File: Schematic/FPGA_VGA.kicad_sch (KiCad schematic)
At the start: 16 parts, among them J1 Conn_01x06, U1 Upduino_3.0, Y1 25.175 MHz 7050 3.3V

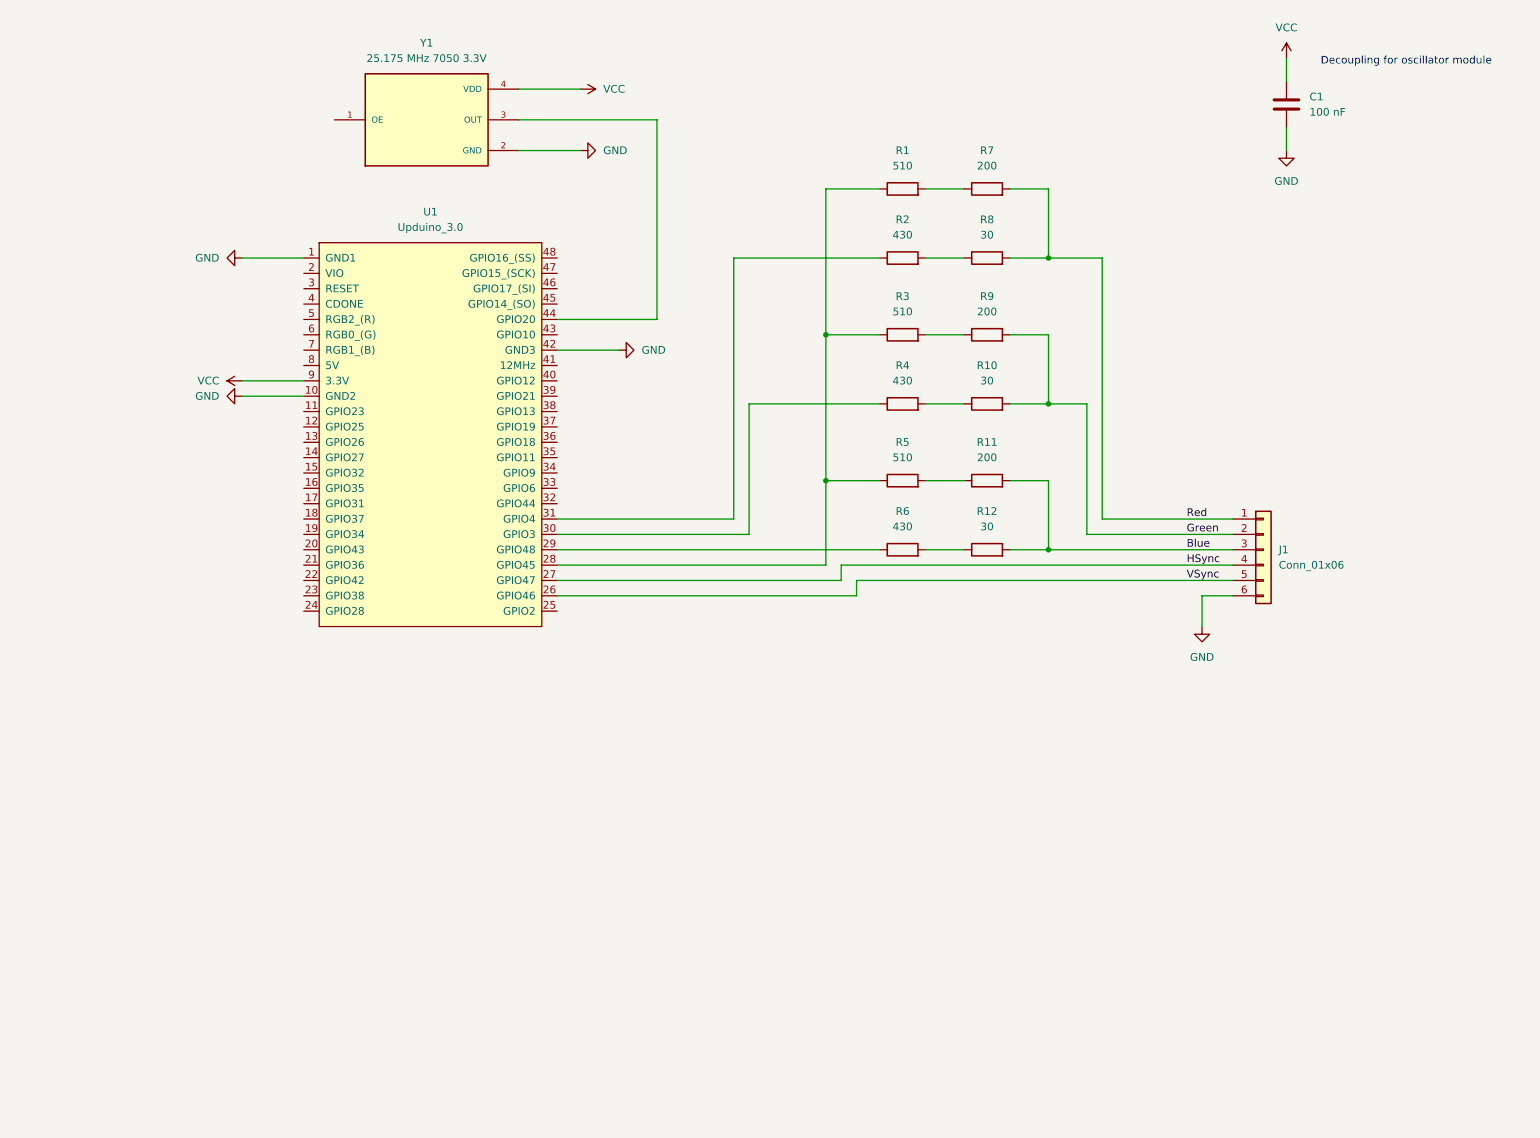
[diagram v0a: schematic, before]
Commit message: start to add level translators for host interface
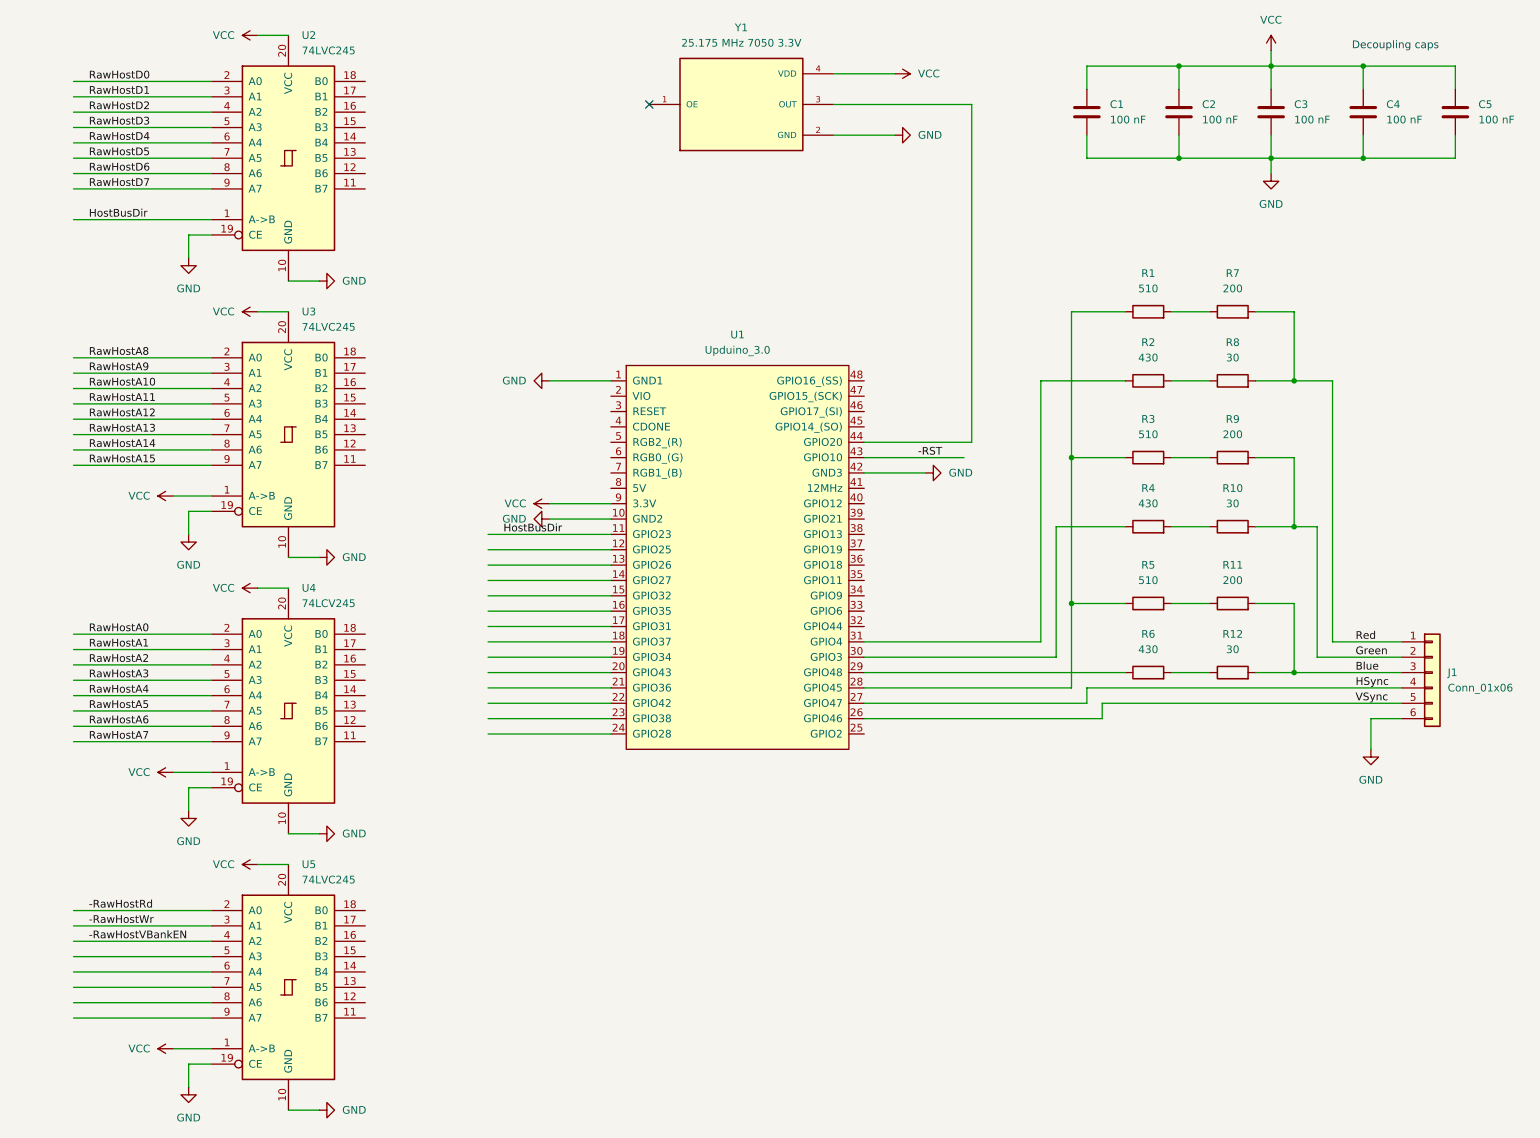
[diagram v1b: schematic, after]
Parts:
- added C2, C3, C4, C5: 100 nF, symbol Device:C
- added U2, U3, U5: 74LVC245, symbol 74xx:74LS245
- added U4: 74LCV245, symbol 74xx:74LS245
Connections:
- net GND: now also C2.2, C3.2, C4.2, C5.2, U2.10 (GND), U2.19 (CE), U3.10 (GND), U3.19 (CE), U4.10 (GND), U4.19 (CE), U5.10 (GND), U5.19 (CE)
- net VCC: now also C2.1, C3.1, C4.1, C5.1, U2.20 (VCC), U3.1 (A->B), U3.20 (VCC), U4.1 (A->B), U4.20 (VCC), U5.1 (A->B), U5.20 (VCC)
- net HostBusDir: now reaches U1.11 (GPIO23)
- net HostBusDir: now also U2.1 (A->B)
- net -RST: now reaches U1.43 (GPIO10)
- new net -RawHostRd: U5.2 (A0)
- new net -RawHostVBankEN: U5.4 (A2)
- new net -RawHostWr: U5.3 (A1)
- new net RawHostA0: U4.2 (A0)
- new net RawHostA1: U4.3 (A1)
- new net RawHostA10: U3.4 (A2)
- new net RawHostA11: U3.5 (A3)
- new net RawHostA12: U3.6 (A4)
- new net RawHostA13: U3.7 (A5)
- new net RawHostA14: U3.8 (A6)
- new net RawHostA15: U3.9 (A7)
- new net RawHostA2: U4.4 (A2)
- new net RawHostA3: U4.5 (A3)
- new net RawHostA4: U4.6 (A4)
- new net RawHostA5: U4.7 (A5)
- new net RawHostA6: U4.8 (A6)
- new net RawHostA7: U4.9 (A7)
- new net RawHostA8: U3.2 (A0)
- new net RawHostA9: U3.3 (A1)
- new net RawHostD0: U2.2 (A0)
- new net RawHostD1: U2.3 (A1)
- new net RawHostD2: U2.4 (A2)
- new net RawHostD3: U2.5 (A3)
- new net RawHostD4: U2.6 (A4)
- new net RawHostD5: U2.7 (A5)
- new net RawHostD6: U2.8 (A6)
- new net RawHostD7: U2.9 (A7)
- no-connect marks 0 -> 1
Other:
- note added: "Decoupling caps"
- note removed: "Decoupling for oscillator module"
- moved on the sheet: C1, J1, R1, R10, R11, R12, R2, R3, R4, R5, R6, R7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

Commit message: added a host interface
Also, modularized the schematic.
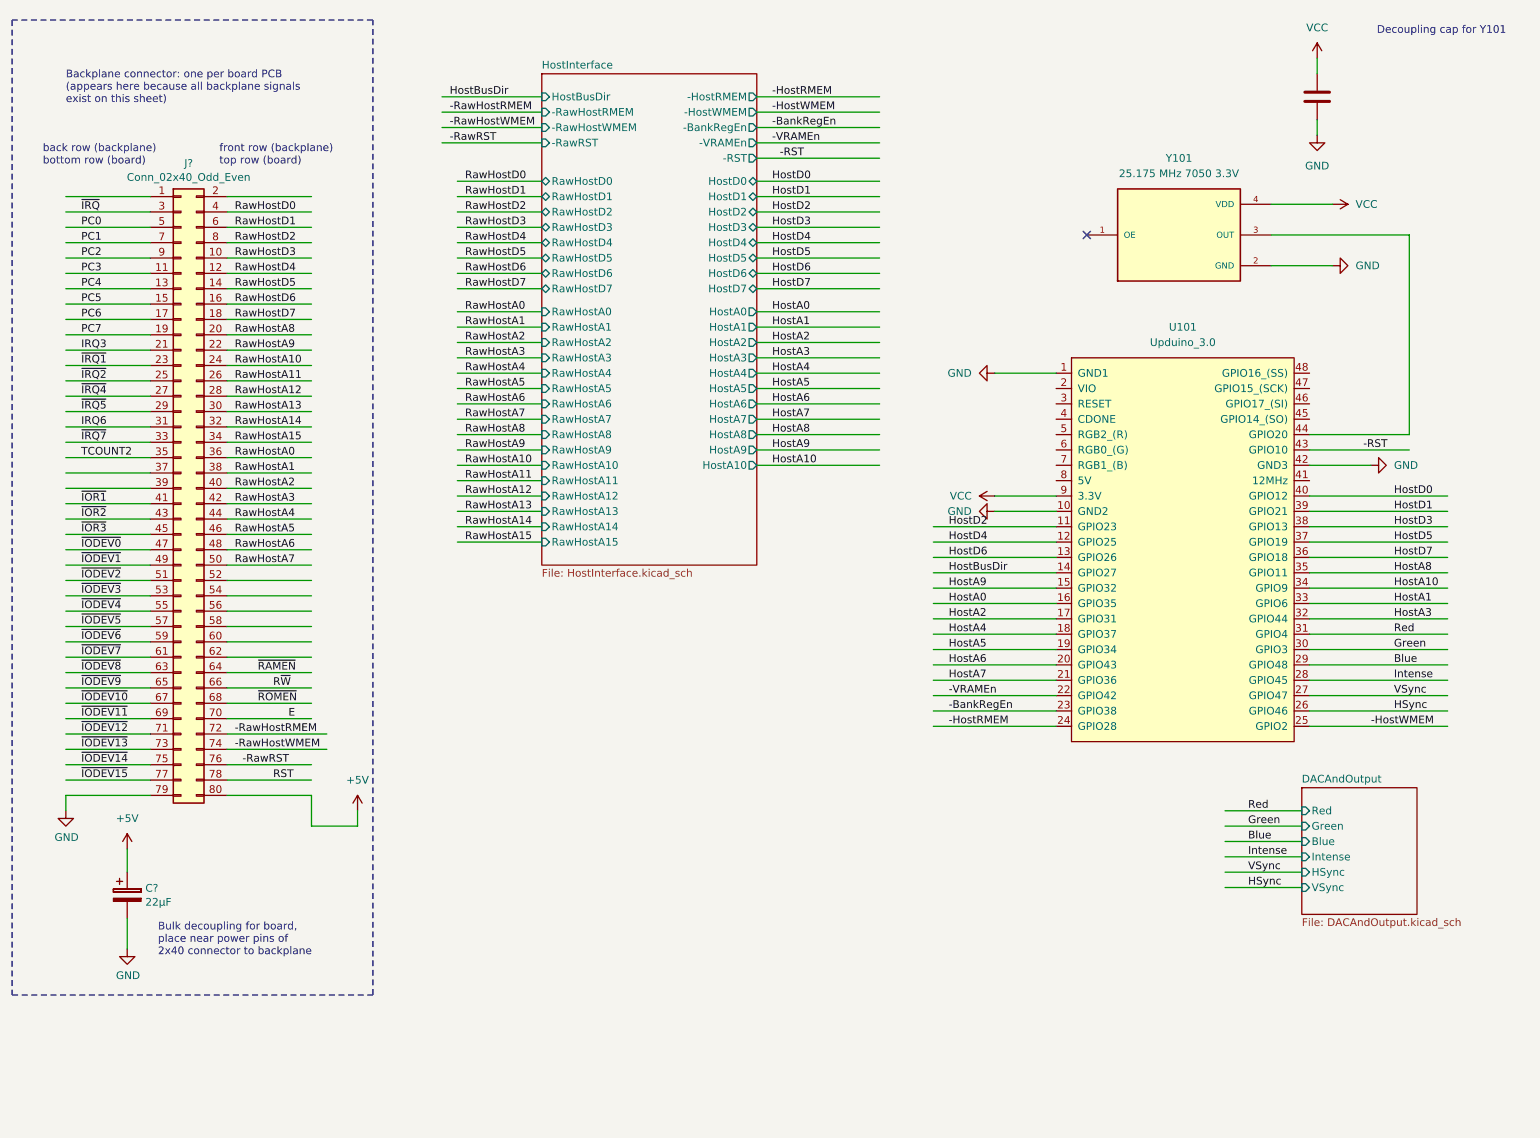
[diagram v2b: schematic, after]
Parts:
- removed C1, C2, C3, C4, C5: 100 nF, symbol Device:C
- removed J1: Conn_01x06, symbol Connector_Generic:Conn_01x06
- removed R1, R3, R5: 510, symbol Device:R
- removed R10, R12, R8: 30, symbol Device:R
- removed R11, R7, R9: 200, symbol Device:R
- removed R2, R4, R6: 430, symbol Device:R
- removed U1: Upduino_3.0, symbol Upduino_3.0:Upduino_3.0
- removed U2, U3, U5: 74LVC245, symbol 74xx:74LS245
- removed U4: 74LCV245, symbol 74xx:74LS245
- removed Y1: 25.175 MHz 7050 3.3V, SIT8208AI-8F-33E-14.745600Y:OSC_SIT8208AI-8F-33E-14.745600Y, symbol SIT8208AI-8F-33E-14.745600Y:SIT8208AI-8F-33E-14.745600Y
- added C?: 100 nF, symbol Device:C
- added C?: 22μF, Capacitor_THT:CP_Radial_D6.3mm_P2.50mm, symbol device:CP
- added J?: Conn_02x40_Odd_Even, Connector_PinHeader_2.54mm:PinHeader_2x40_P2.54mm_Vertical, symbol Connector_Generic:Conn_02x40_Odd_Even
- added U101: Upduino_3.0, symbol Upduino_3.0:Upduino_3.0
- added Y101: 25.175 MHz 7050 3.3V, SIT8208AI-8F-33E-14.745600Y:OSC_SIT8208AI-8F-33E-14.745600Y, symbol SIT8208AI-8F-33E-14.745600Y:SIT8208AI-8F-33E-14.745600Y
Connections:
- net -RST: now also U101.43 (GPIO10)
- net Blue: now also U101.29 (GPIO48)
- net GND: now also C?.2, C?.2, J?.79 (Pin_79), U101.1 (GND1), U101.10 (GND2), U101.42 (GND3), Y101.2 (GND)
- net Green: now also U101.30 (GPIO3)
- net HSync: now also U101.26 (GPIO46)
- net HostBusDir: now also U101.14 (GPIO27)
- net RawHostA0: now also J?.36 (Pin_36)
- net RawHostA1: now also J?.38 (Pin_38)
- net RawHostA10: now also J?.24 (Pin_24)
- net RawHostA11: now also J?.26 (Pin_26)
- net RawHostA12: now also J?.28 (Pin_28)
- net RawHostA13: now also J?.30 (Pin_30)
- net RawHostA14: now also J?.32 (Pin_32)
- net RawHostA15: now also J?.34 (Pin_34)
- net RawHostA2: now also J?.40 (Pin_40)
- net RawHostA3: now also J?.42 (Pin_42)
- net RawHostA4: now also J?.44 (Pin_44)
- net RawHostA5: now also J?.46 (Pin_46)
- net RawHostA6: now also J?.48 (Pin_48)
- net RawHostA7: now also J?.50 (Pin_50)
- net RawHostA8: now also J?.20 (Pin_20)
- net RawHostA9: now also J?.22 (Pin_22)
- net RawHostD0: now also J?.4 (Pin_4)
- net RawHostD1: now also J?.6 (Pin_6)
- net RawHostD2: now also J?.8 (Pin_8)
- net RawHostD3: now also J?.10 (Pin_10)
- net RawHostD4: now also J?.12 (Pin_12)
- net RawHostD5: now also J?.14 (Pin_14)
- net RawHostD6: now also J?.16 (Pin_16)
- net RawHostD7: now also J?.18 (Pin_18)
- net Red: now also U101.31 (GPIO4)
- net VCC: now also C?.1, U101.9 (3.3V), Y101.4 (VDD)
- net VSync: now also U101.27 (GPIO47)
- new net: U101.44 (GPIO20), Y101.3 (OUT)
- new net +5V: C?.1, J?.80 (Pin_80)
- new net -BankRegEn: U101.23 (GPIO38)
- new net -HostRMEM: U101.24 (GPIO28)
- new net -HostWMEM: U101.25 (GPIO2)
- new net -RawHostRMEM: J?.72 (Pin_72)
- new net -RawHostWMEM: J?.74 (Pin_74)
- new net -RawRST: J?.76 (Pin_76)
- new net -VRAMEn: U101.22 (GPIO42)
- new net E: J?.70 (Pin_70)
- new net HostA0: U101.16 (GPIO35)
- new net HostA1: U101.33 (GPIO6)
- new net HostA10: U101.34 (GPIO9)
- new net HostA2: U101.17 (GPIO31)
- new net HostA3: U101.32 (GPIO44)
- new net HostA4: U101.18 (GPIO37)
- new net HostA5: U101.19 (GPIO34)
- new net HostA6: U101.20 (GPIO43)
- new net HostA7: U101.21 (GPIO36)
- new net HostA8: U101.35 (GPIO11)
- new net HostA9: U101.15 (GPIO32)
- new net HostD0: U101.40 (GPIO12)
- new net HostD1: U101.39 (GPIO21)
- new net HostD2: U101.11 (GPIO23)
- new net HostD3: U101.38 (GPIO13)
- new net HostD4: U101.12 (GPIO25)
- new net HostD5: U101.37 (GPIO19)
- new net HostD6: U101.13 (GPIO26)
- new net HostD7: U101.36 (GPIO18)
- new net IRQ3: J?.21 (Pin_21)
- new net IRQ6: J?.31 (Pin_31)
- new net Intense: U101.28 (GPIO45)
- new net PC0: J?.5 (Pin_5)
- new net PC1: J?.7 (Pin_7)
- new net PC2: J?.9 (Pin_9)
- new net PC3: J?.11 (Pin_11)
- new net PC4: J?.13 (Pin_13)
- new net PC5: J?.15 (Pin_15)
- new net PC6: J?.17 (Pin_17)
- new net PC7: J?.19 (Pin_19)
- new net RST: J?.78 (Pin_78)
- new net R~{W}: J?.66 (Pin_66)
- new net TCOUNT2: J?.35 (Pin_35)
- new net ~{IODEV0}: J?.47 (Pin_47)
- new net ~{IODEV10}: J?.67 (Pin_67)
- new net ~{IODEV11}: J?.69 (Pin_69)
- new net ~{IODEV12}: J?.71 (Pin_71)
- new net ~{IODEV13}: J?.73 (Pin_73)
- new net ~{IODEV14}: J?.75 (Pin_75)
- new net ~{IODEV15}: J?.77 (Pin_77)
- new net ~{IODEV1}: J?.49 (Pin_49)
- new net ~{IODEV2}: J?.51 (Pin_51)
- new net ~{IODEV3}: J?.53 (Pin_53)
- new net ~{IODEV4}: J?.55 (Pin_55)
- new net ~{IODEV5}: J?.57 (Pin_57)
- new net ~{IODEV6}: J?.59 (Pin_59)
- new net ~{IODEV7}: J?.61 (Pin_61)
- new net ~{IODEV8}: J?.63 (Pin_63)
- new net ~{IODEV9}: J?.65 (Pin_65)
- new net ~{IOR1}: J?.41 (Pin_41)
- new net ~{IOR2}: J?.43 (Pin_43)
- new net ~{IOR3}: J?.45 (Pin_45)
- new net ~{IRQ1}: J?.23 (Pin_23)
- new net ~{IRQ2}: J?.25 (Pin_25)
- new net ~{IRQ4}: J?.27 (Pin_27)
- new net ~{IRQ5}: J?.29 (Pin_29)
- new net ~{IRQ7}: J?.33 (Pin_33)
- new net ~{IRQ}: J?.3 (Pin_3)
- new net ~{RAMEN}: J?.64 (Pin_64)
- new net ~{ROMEN}: J?.68 (Pin_68)
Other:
- added sheet DACAndOutput (DACAndOutput.kicad_sch)
- added sheet HostInterface (HostInterface.kicad_sch)
- note added: "Backplane connector: one per board PCB (appears here because all backplane signals exist on this sheet)"
- note added: "Bulk decoupling for board, place near power pins of 2x40 connector to backplane"
- note added: "Decoupling cap for Y101"
- note added: "back row (backplane) bottom row (board)"
- note added: "front row (backplane) top row (board)"
- note removed: "Decoupling caps"
- company: (none) -> daveho hacks
- title: (none) -> FPGA text display
